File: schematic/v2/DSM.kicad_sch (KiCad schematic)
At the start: 10 parts, among them J3 LCD_display, U17 NUCLEO-H753ZI

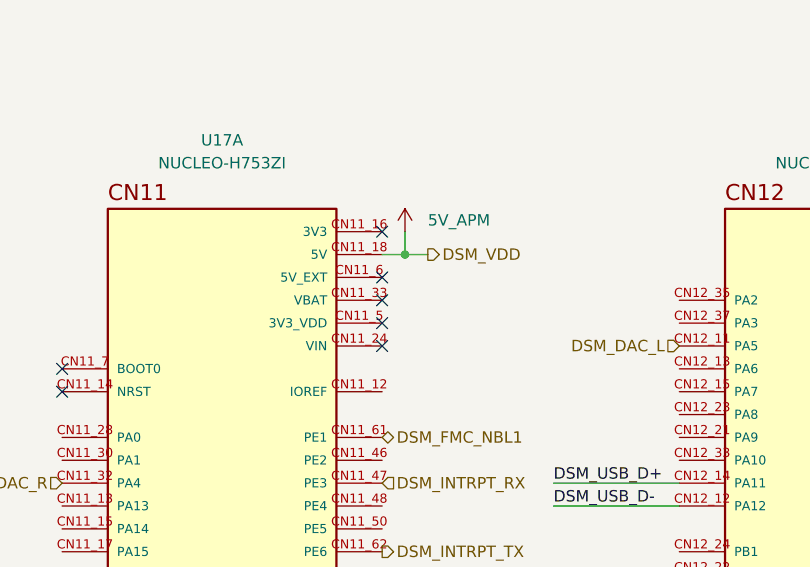
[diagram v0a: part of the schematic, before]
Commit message: schematic updates, no errors at least. running DRC on pcb
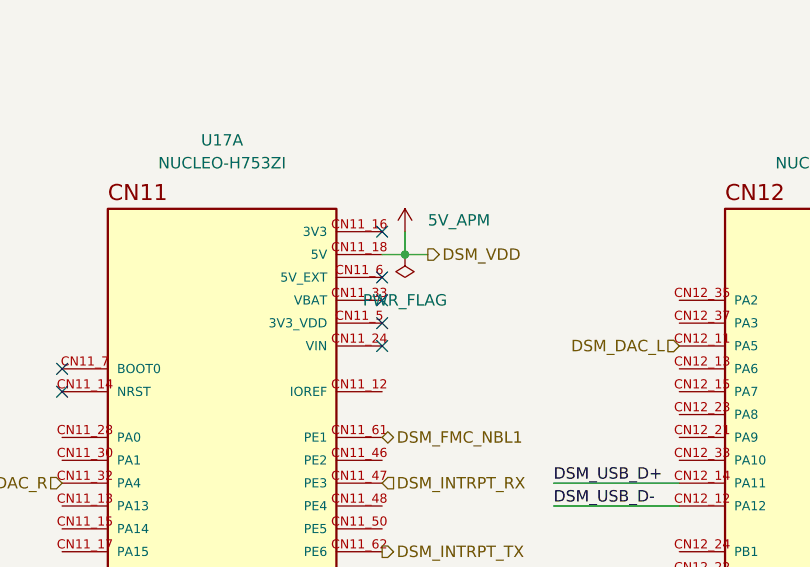
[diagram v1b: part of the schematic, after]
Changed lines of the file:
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@@
+	)
+	(symbol
+		(lib_id "power:PWR_FLAG")
+		(at 146.05 102.87 180)
+		(unit 1)
+		(exclude_from_sim no)
+		(in_bom yes)
+		(on_board yes)
+		(dnp no)
+		(fields_autoplaced yes)
+		(property "Reference" "#FLG04"
+			(at 146.05 104.775 0)
+			(effects
+				(font
+					(size 1.27 1.27)
+				)
+				(hide yes)
+			)
+		)
+		(property "Value" "PWR_FLAG"
+			(at 146.05 107.95 0)
+			(effects
+				(font
+					(size 1.27 1.27)
+				)
+			)
+		)
+		(property "Footprint" ""
+			(at 146.05 102.87 0)
+			(effects
+				(font
+					(size 1.27 1.27)
+				)
+				(hide yes)
+			)
+		)
+		(property "Datasheet" "~"
+			(at 146.05 102.87 0)
+			(effects
+				(font
+					(size 1.27 1.27)
+				)
+				(hide yes)
+			)
+		)
+		(property "Description" "Special symbol for telling ERC where power comes from"
+			(at 146.05 102.87 0)
+			(effects
+				(font
+					(size 1.27 1.27)
+				)
+				(hide yes)
+			)
+		)
+		(pin "1"
+		)
+		(instances
+			(project ""
+				(path "/fe7b15e9-f0ed-4338-9f03-dd7651dace13/4391c51f-6ab5-4b63-a6de-56382e56f1df"
+					(reference "#FLG04")
+					(unit 1)
+				)
+			)
+		)
 	)
 	(symbol

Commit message: some progress on affm board
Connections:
- net 5V_APM renamed 5V_DSM
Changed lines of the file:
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@@
 			)
 		)
-		(property "Value" "5V_APM"
-			(at 148.59 99.0599 0)
+		(property "Value" "5V_DSM"
+			(at 146.05 95.25 0)
 			(effects
 				(font
 					(size 1.27 1.27)
 				)
-				(justify left)
 			)
 		)

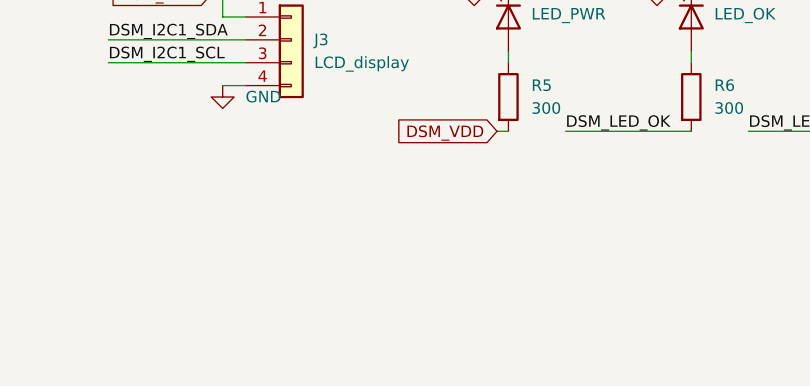
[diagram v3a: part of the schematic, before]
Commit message: now making a v3 with HATs for each nucleo with my needed shit. this will make things very compact and hopefully much cheaper
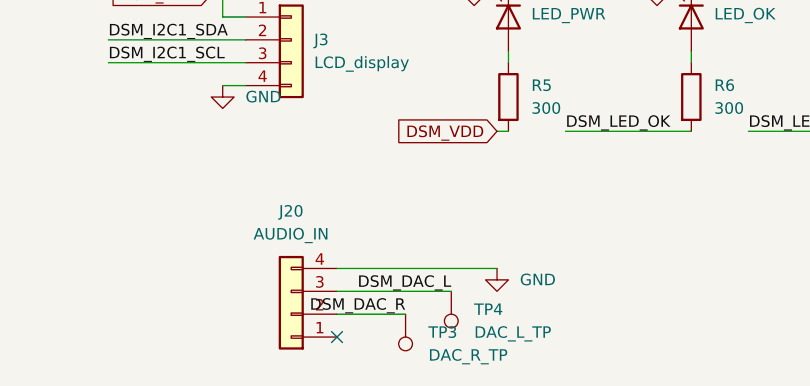
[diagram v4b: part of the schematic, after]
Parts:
- added J20: AUDIO_IN, Connector:NS-Tech_Grove_1x04_P2mm_Vertical, symbol Connector_Generic:Conn_01x04
- added TP3: DAC_R_TP, TestPoint:TestPoint_THTPad_D2.5mm_Drill1.2mm, symbol Connector:TestPoint
- added TP4: DAC_L_TP, TestPoint:TestPoint_THTPad_D2.5mm_Drill1.2mm, symbol Connector:TestPoint
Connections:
- net DSM_DAC_L: now also J20.3 (Pin_3), TP4.1
- net DSM_DAC_R: now also J20.2 (Pin_2), TP3.1
- net GND: now also J20.4 (Pin_4)
- no-connect marks 11 -> 12
